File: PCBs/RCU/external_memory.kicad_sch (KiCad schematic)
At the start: 2 parts

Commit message: Replaced Bidrectional TVS diodes with USBLC-2SC6 unidirectional ESD protection
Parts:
- U?: value (none) -> SST26VF032BT-104I/SM; footprint (none) -> Package_SO:SOIC-8_5.275x5.275mm_P1.27mm
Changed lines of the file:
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@@
     (in_bom yes) (on_board yes)
     (property "Reference" "U?" (id 0) (at 93.98 78.74 0))
-    (property "Value" "" (id 1) (at 76.2 81.28 0))
-    (property "Footprint" "" (id 2) (at 90.17 87.63 0)
+    (property "Value" "SST26VF032BT-104I/SM" (id 1) (at 76.2 81.28 0))
+    (property "Footprint" "Package_SO:SOIC-8_5.275x5.275mm_P1.27mm" (id 2) (at 90.17 87.63 0)
       (effects (font (size 1.27 1.27)) hide)
     )

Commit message: Full annoted external memory schematic
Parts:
- gave numbers to parts that had none: 2
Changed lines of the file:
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@@
   (symbol (lib_id "Device:C") (at 123.19 69.85 0) (unit 1)
     (in_bom yes) (on_board yes) (fields_autoplaced)
-    (property "Reference" "C?" (id 0) (at 127 68.5799 0)
+    (property "Reference" "C700" (id 0) (at 127 68.5799 0)
       (effects (font (size 1.27 1.27)) (justify left))
     )
@@
   (symbol (lib_id "Memory_Flash:SST25VF080B-50-4x-S2Ax") (at 90.17 69.85 0) (unit 1)
     (in_bom yes) (on_board yes)
-    (property "Reference" "U?" (id 0) (at 93.98 78.74 0))
+    (property "Reference" "U700" (id 0) (at 93.98 78.74 0))
     (property "Value" "SST26VF032BT-104I/SM" (id 1) (at 76.2 81.28 0))
     (property "Footprint" "Package_SO:SOIC-8_5.275x5.275mm_P1.27mm" (id 2) (at 90.17 87.63 0)

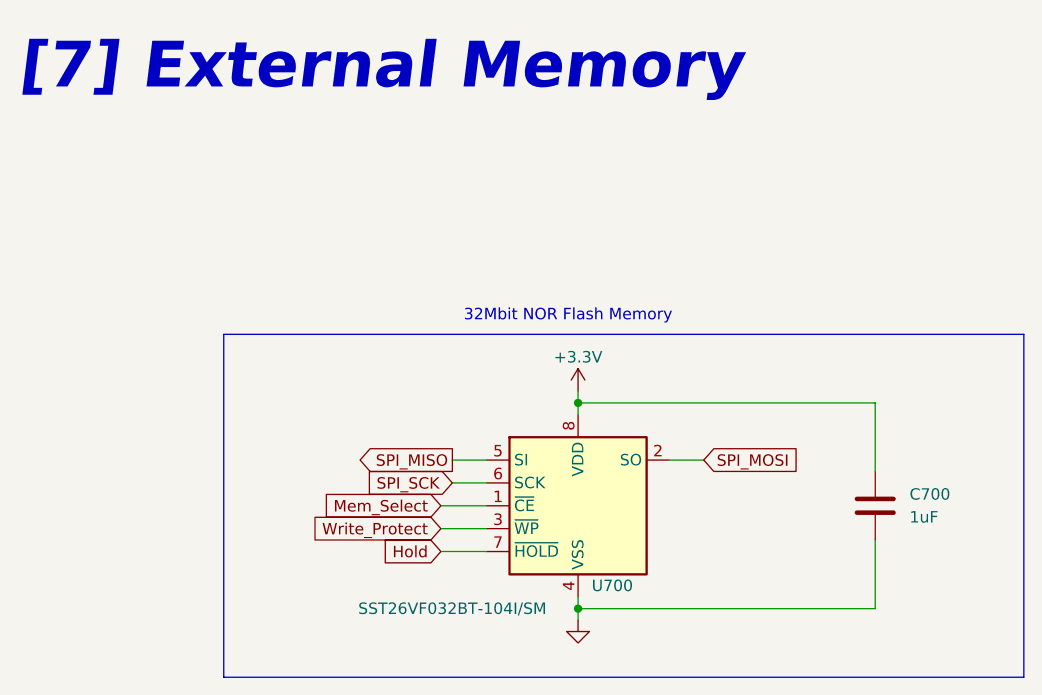
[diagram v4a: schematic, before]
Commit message: Corrected SPI_MOSI and SPI_MISO labels on U700 - external memory
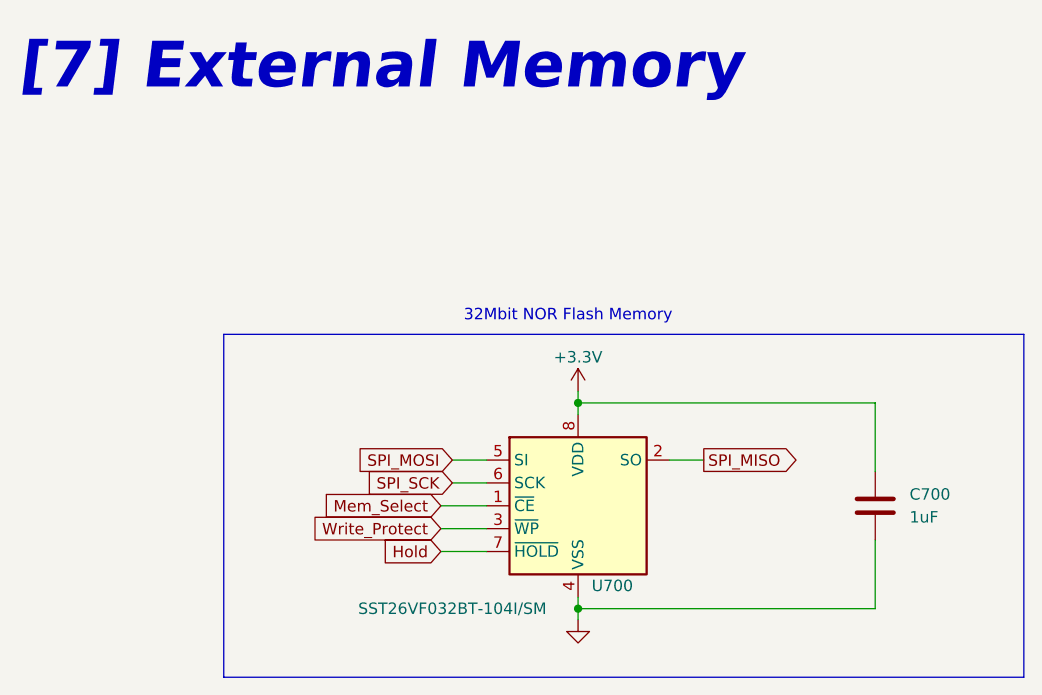
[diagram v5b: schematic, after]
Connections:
- net SPI_MISO: now also U700.2 (SO); no longer U700.5 (SI)
- net SPI_MOSI: now also U700.5 (SI); no longer U700.2 (SO)
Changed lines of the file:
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@@
+    (stroke (width 0) (type default) (color 0 0 0 0))
+  )
+  (wire (pts (xy 104.14 64.77) (xy 100.33 64.77))
     (stroke (width 0) (type default) (color 0 0 0 0))
   )
@@
     (stroke (width 0) (type default) (color 0 0 0 0))
   )
+  (wire (pts (xy 76.2 64.77) (xy 80.01 64.77))
+    (stroke (width 0) (type default) (color 0 0 0 0))
+  )
   (polyline (pts (xy 50.8 88.9) (xy 139.7 88.9))
     (stroke (width 0) (type default) (color 0 0 0 0))
   )
   (wire (pts (xy 90.17 58.42) (xy 90.17 59.69))
-    (stroke (width 0) (type default) (color 0 0 0 0))
-  )
-  (wire (pts (xy 104.14 64.77) (xy 100.33 64.77))
-    (stroke (width 0) (type default) (color 0 0 0 0))
-  )
-  (wire (pts (xy 76.2 64.77) (xy 80.01 64.77))
     (stroke (width 0) (type default) (color 0 0 0 0))
   )
@@
     )
   )
-  (global_label "SPI_MOSI" (shape input) (at 104.14 64.77 0) (fields_autoplaced)
-    (effects (font (size 1.27 1.27)) (justify left))
-    (property "Intersheet References" "${INTERSHEET_REFS}" (id 0) (at 115.2012 64.6906 0)
-      (effects (font (size 1.27 1.27)) (justify left) hide)
-    )
-  )
   (global_label "Write_Protect" (shape input) (at 74.93 72.39 180) (fields_autoplaced)
     (effects (font (size 1.27 1.27)) (justify right))
@@
     )
   )
-  (global_label "SPI_MISO" (shape output) (at 76.2 64.77 180) (fields_autoplaced)
+  (global_label "SPI_MOSI" (shape input) (at 76.2 64.77 180) (fields_autoplaced)
     (effects (font (size 1.27 1.27)) (justify right))
     (property "Intersheet References" "${INTERSHEET_REFS}" (id 0) (at 65.1388 64.6906 0)
@@
     )
   )
+  (global_label "SPI_MISO" (shape output) (at 104.14 64.77 0) (fields_autoplaced)
+    (effects (font (size 1.27 1.27)) (justify left))
+    (property "Intersheet References" "${INTERSHEET_REFS}" (id 0) (at 115.2012 64.6906 0)
+      (effects (font (size 1.27 1.27)) (justify left) hide)
+    )
+  )

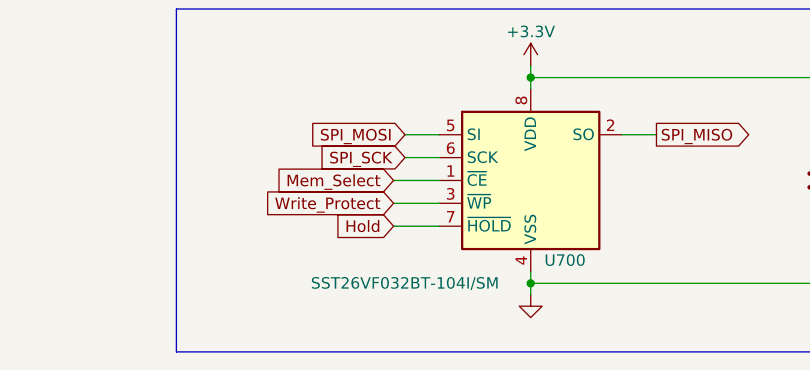
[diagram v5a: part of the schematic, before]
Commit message: Add footprint to rest of IC's except ESP32
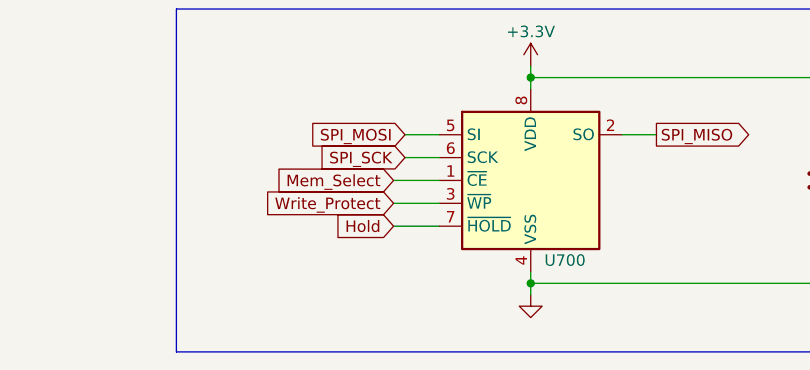
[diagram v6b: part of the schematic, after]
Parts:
- U700: value SST26VF032BT-104I/SM -> (none); footprint Package_SO:SOIC-8_5.275x5.275mm_P1.27mm -> (none)
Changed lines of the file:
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@@
     (in_bom yes) (on_board yes)
     (property "Reference" "U700" (id 0) (at 93.98 78.74 0))
-    (property "Value" "SST26VF032BT-104I/SM" (id 1) (at 76.2 81.28 0))
-    (property "Footprint" "Package_SO:SOIC-8_5.275x5.275mm_P1.27mm" (id 2) (at 90.17 87.63 0)
+    (property "Value" "" (id 1) (at 76.2 81.28 0))
+    (property "Footprint" "" (id 2) (at 90.17 87.63 0)
       (effects (font (size 1.27 1.27)) hide)
     )

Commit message: Add footprint to power module diodes, and replaced 1N4148W with 2 SM5817's
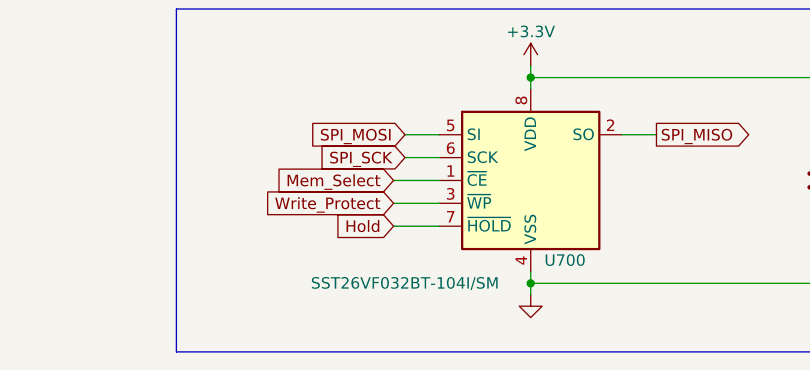
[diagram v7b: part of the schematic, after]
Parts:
- U700: value (none) -> SST26VF032BT-104I/SM; footprint (none) -> Package_SO:SOIC-8_5.275x5.275mm_P1.27mm
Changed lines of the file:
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@@
     (in_bom yes) (on_board yes)
     (property "Reference" "U700" (id 0) (at 93.98 78.74 0))
-    (property "Value" "" (id 1) (at 76.2 81.28 0))
-    (property "Footprint" "" (id 2) (at 90.17 87.63 0)
+    (property "Value" "SST26VF032BT-104I/SM" (id 1) (at 76.2 81.28 0))
+    (property "Footprint" "Package_SO:SOIC-8_5.275x5.275mm_P1.27mm" (id 2) (at 90.17 87.63 0)
       (effects (font (size 1.27 1.27)) hide)
     )

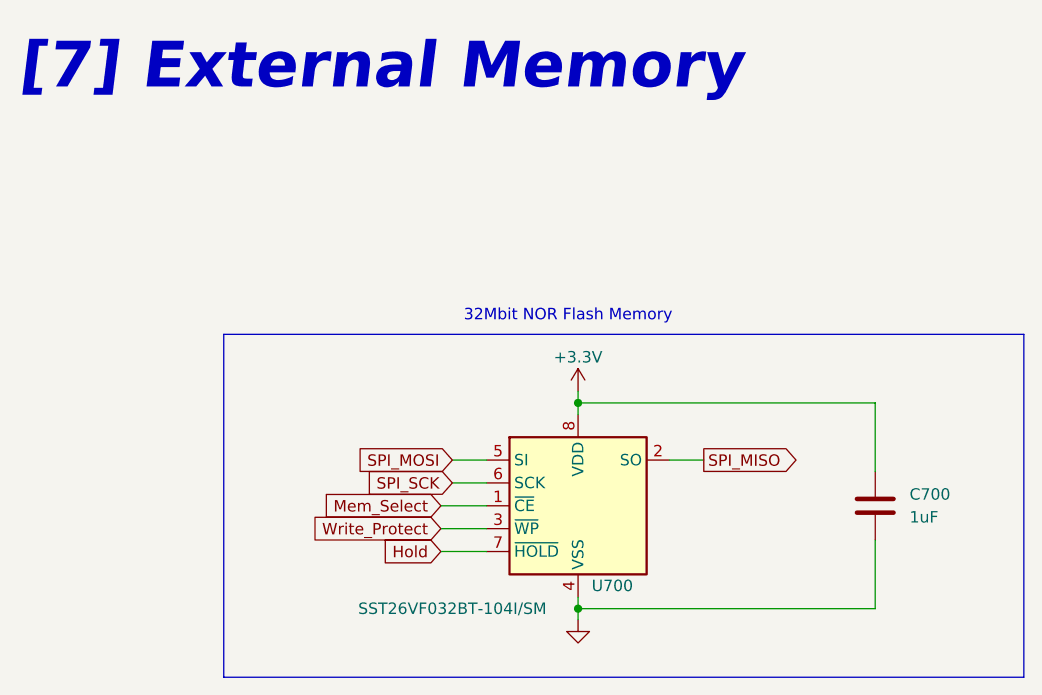
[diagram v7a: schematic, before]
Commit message: Add footrpints to TVS diodes in [3]
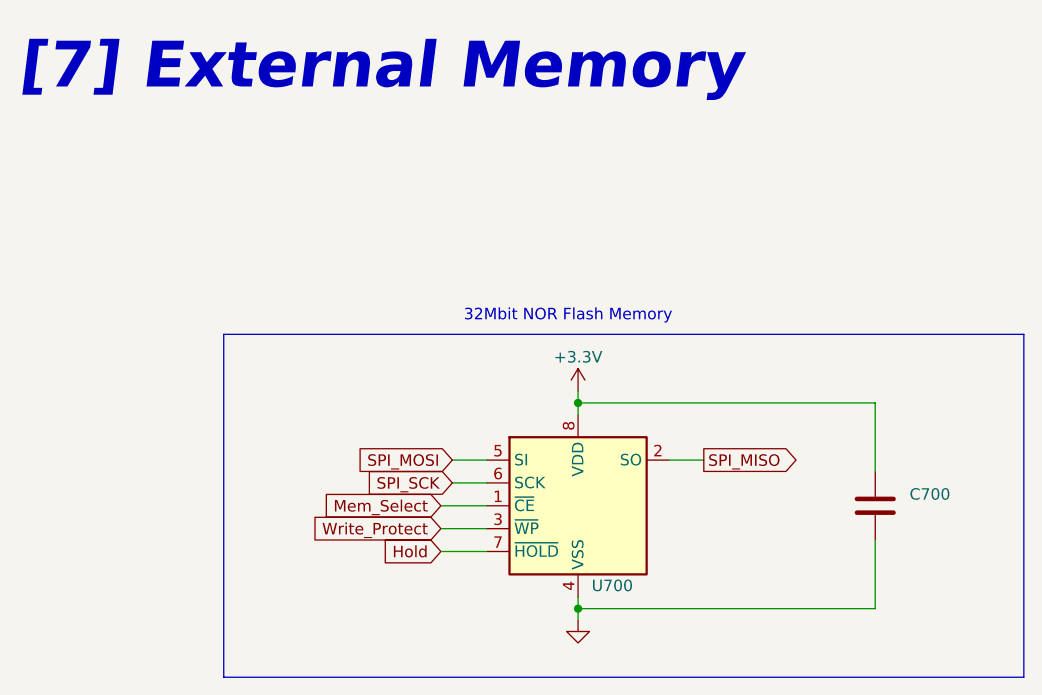
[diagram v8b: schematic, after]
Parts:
- C700: value 1uF -> (none)
- U700: value SST26VF032BT-104I/SM -> (none); footprint Package_SO:SOIC-8_5.275x5.275mm_P1.27mm -> (none)
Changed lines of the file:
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@@
   (symbol (lib_id "power:+3.3V") (at 90.17 57.15 0) (unit 1)
     (in_bom yes) (on_board yes)
-    (property "Reference" "#PWR?" (id 0) (at 90.17 60.96 0)
+    (property "Reference" "#PWR0202" (id 0) (at 90.17 60.96 0)
       (effects (font (size 1.27 1.27)) hide)
     )
@@
       (effects (font (size 1.27 1.27)) (justify left))
     )
-    (property "Value" "1uF" (id 1) (at 127 71.1199 0)
+    (property "Value" "" (id 1) (at 127 71.1199 0)
       (effects (font (size 1.27 1.27)) (justify left))
     )
@@
   (symbol (lib_id "power:GND") (at 90.17 82.55 0) (unit 1)
     (in_bom yes) (on_board yes) (fields_autoplaced)
-    (property "Reference" "#PWR?" (id 0) (at 90.17 88.9 0)
+    (property "Reference" "#PWR0201" (id 0) (at 90.17 88.9 0)
       (effects (font (size 1.27 1.27)) hide)
     )
@@
     (in_bom yes) (on_board yes)
     (property "Reference" "U700" (id 0) (at 93.98 78.74 0))
-    (property "Value" "SST26VF032BT-104I/SM" (id 1) (at 76.2 81.28 0))
-    (property "Footprint" "Package_SO:SOIC-8_5.275x5.275mm_P1.27mm" (id 2) (at 90.17 87.63 0)
+    (property "Value" "" (id 1) (at 76.2 81.28 0))
+    (property "Footprint" "" (id 2) (at 90.17 87.63 0)
       (effects (font (size 1.27 1.27)) hide)
     )
